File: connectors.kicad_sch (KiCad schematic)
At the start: 41 parts, among them J1 Conn_01x06, J10 Conn_01x06, J11 24V, J12 24V, J13 SIGNAL, J14 GND, J15 GND, J16 Conn_01x06, J17 Conn_01x06, J2 Conn_01x06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

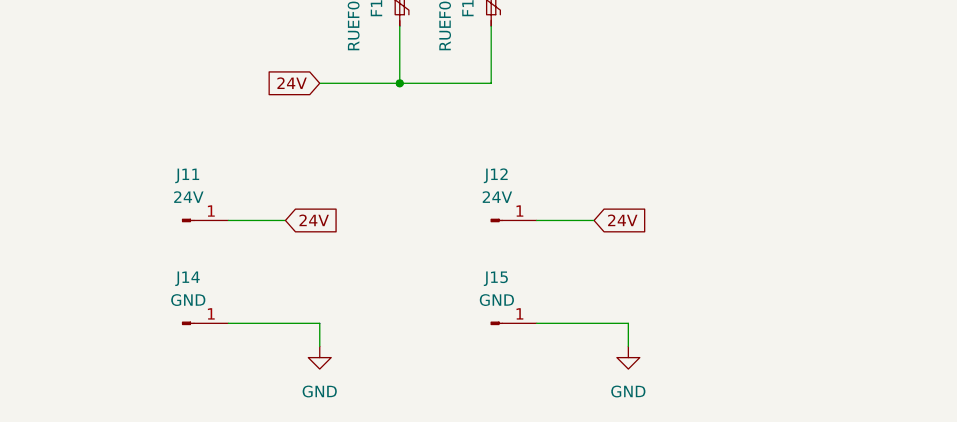
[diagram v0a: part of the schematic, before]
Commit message: finish p1 board layout
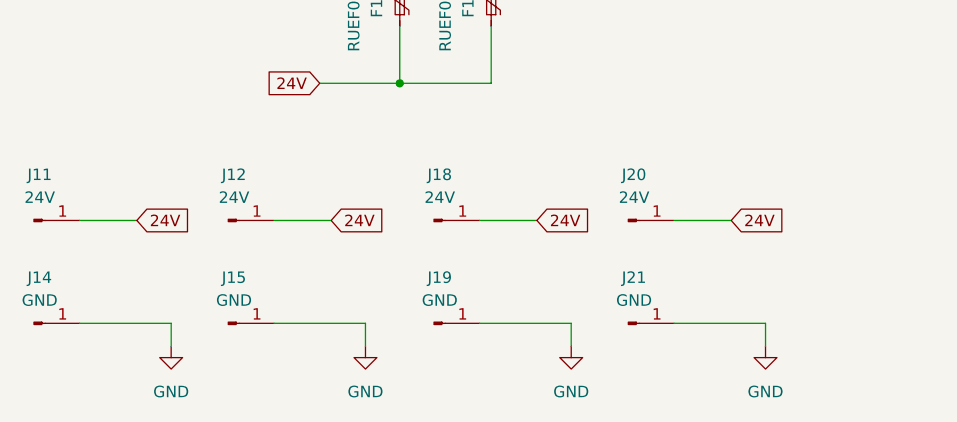
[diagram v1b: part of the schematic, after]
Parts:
- added J18, J20: 24V, Library:1212, symbol Connector:Conn_01x01_Male
- added J19, J21: GND, Library:1212, symbol Connector:Conn_01x01_Male
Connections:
- net 24V: now also J18.1 (Pin_1), J20.1 (Pin_1)
- net GND: now also J19.1 (Pin_1), J21.1 (Pin_1)
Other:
- moved on the sheet: J11, J12, J14, J15
